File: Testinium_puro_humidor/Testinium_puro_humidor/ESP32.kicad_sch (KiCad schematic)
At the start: 0 parts

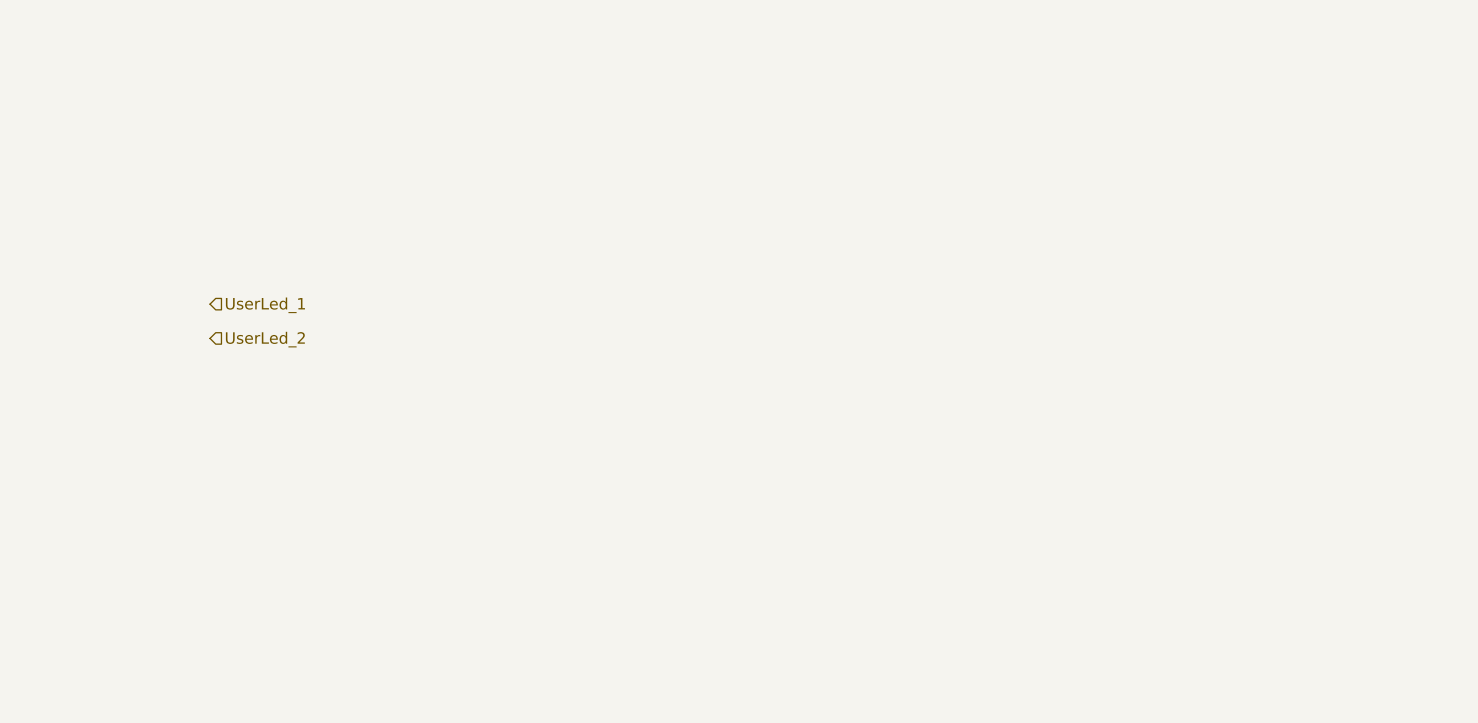
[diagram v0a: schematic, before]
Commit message: fan , uv led ,regülator devresi eklendi. piezo ve sarj devresi kaldi
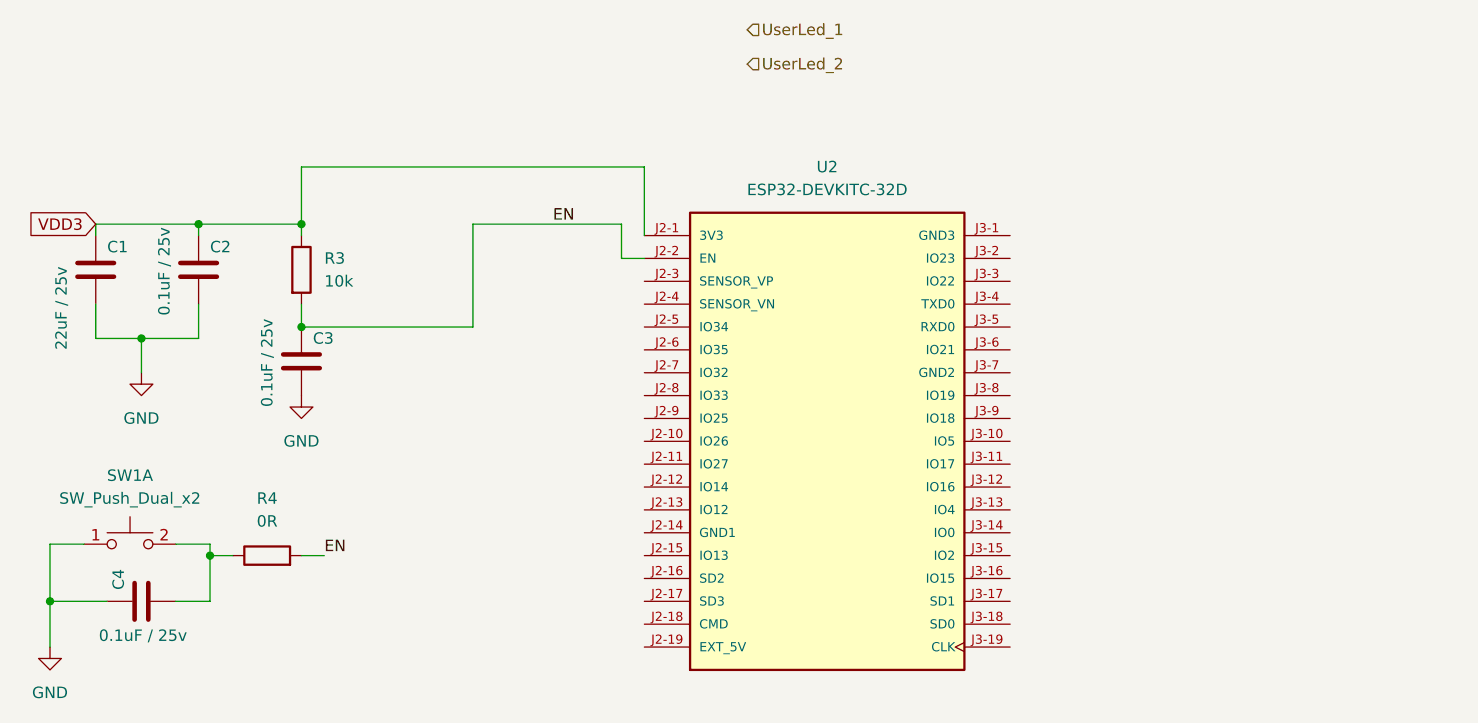
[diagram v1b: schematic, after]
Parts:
- added C1: 22uF / 25v, symbol Device:C
- added C2, C3, C4: 0.1uF / 25v, symbol Device:C
- added R3: 10k, symbol Device:R
- added R4: 0R, symbol Device:R
- added SW1: SW_Push_Dual_x2, symbol Switch:SW_Push_Dual_x2
- added U2: ESP32-DEVKITC-32D, baraysan:pin_header_esp32, symbol BARAYSAN:ESP32-DEVKITC-32D
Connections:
- new net: C4.2, R4.1, SW1.2 (D)
- new net EN: C3.1, R3.2, R4.2, U2.J2-2 (EN)
- new net GND: C1.2, C2.2, C3.2, C4.1, SW1.1 (C)
- new net VDD3: C1.1, C2.1, R3.1, U2.J2-1 (3V3)

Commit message: sematik tamamlandi
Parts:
- removed C4: 0.1uF / 25v, symbol Device:C
- removed R4: 0R, symbol Device:R
- removed SW1: SW_Push_Dual_x2, symbol Switch:SW_Push_Dual_x2
- added R17, R18, R19, R20: 4K7, Resistor_SMD:R_0805_2012Metric, symbol Device:R
- C1, C2, C3: footprint (none) -> Capacitor_SMD:C_0805_2012Metric
- R3: footprint (none) -> Resistor_SMD:R_0805_2012Metric
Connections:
- net I2C0_SCL: now reaches U2.J3-13 (IO4)
- net I2C0_SCL: now also R18.1
- net I2C0_SDA: now reaches U2.J3-14 (IO0)
- net I2C0_SDA: now also R17.1
- net I2C1_SDA: now reaches U2.J3-17 (SD1)
- net I2C1_SDA: now also R19.1
- net I2C1_SCL: now reaches U2.J3-18 (SD0)
- net I2C1_SCL: now also R20.1
- new net +3V3: R17.2, R18.2, R19.2, R20.2
